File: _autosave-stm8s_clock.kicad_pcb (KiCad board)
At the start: 2 copper layers, 157 parts, among them J1 Conn_01x04, J2 PS, Q1 BC847, Q10 BC847, Q11 BC847, Q12 BC847, Q13 BC847, Q14 BC847, Q15 BC847, Q16 BC847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

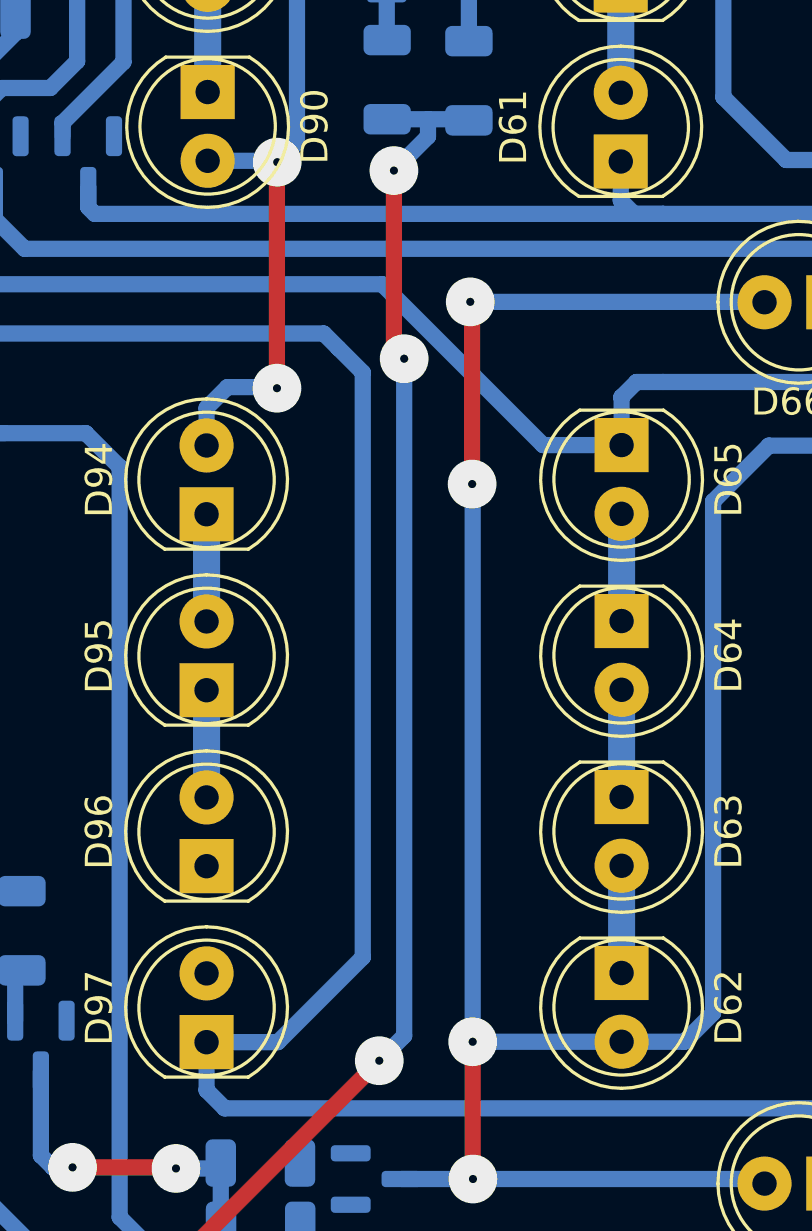
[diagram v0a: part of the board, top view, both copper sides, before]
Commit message: connect to all segment and each digit or shift register to connect each other
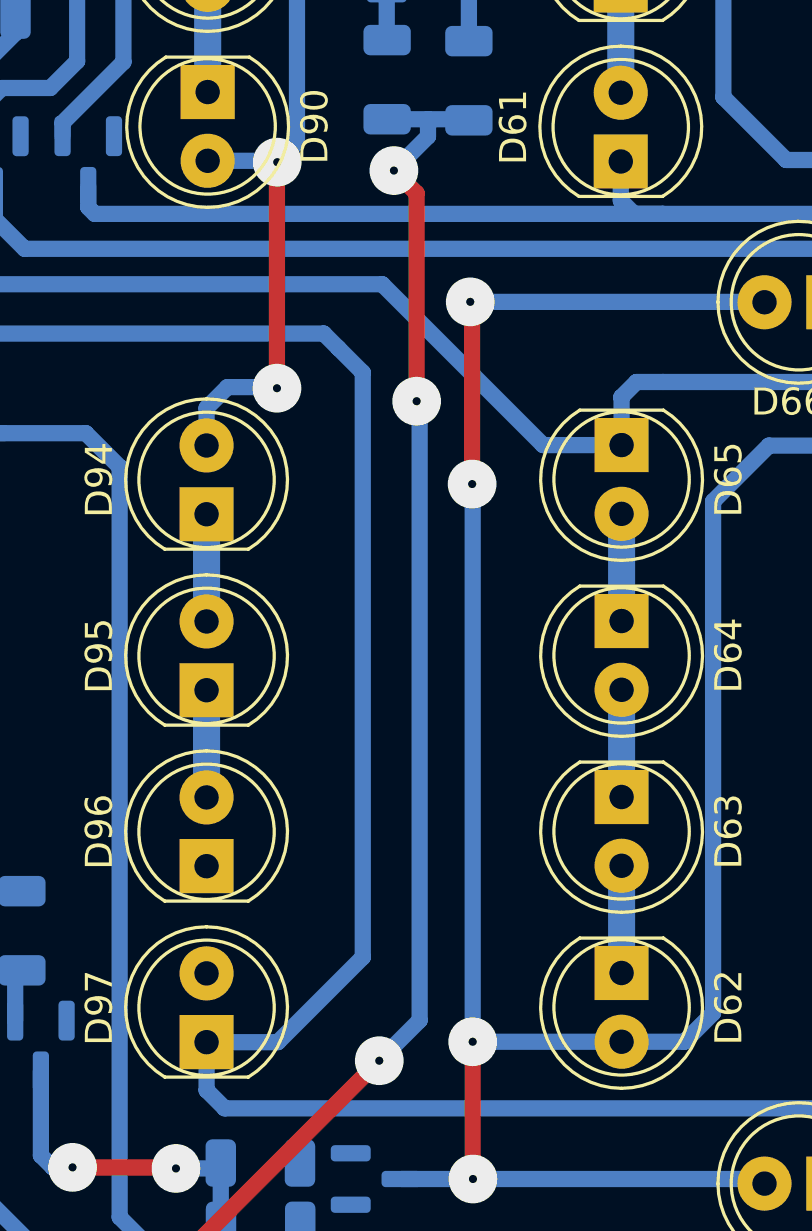
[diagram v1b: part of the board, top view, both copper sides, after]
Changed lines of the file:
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@@
 		(tags "TSSOP SO")
 		(property "Reference" "U1"
-			(at 0 4.2 360)
+			(at 0 4.2 0)
 			(layer "B.SilkS")
 			(effects
@@
 		)
 		(property "Value" "STM8S003F3P"
-			(at 0 -4.2 360)
+			(at 0 -4.2 0)
 			(layer "B.Fab")
 			(effects
@@
 		)
 		(property "Footprint" "Package_SO:TSSOP-20_4.4x6.5mm_P0.65mm"
-			(at 0 0 360)
+			(at 0 0 0)
 			(layer "B.Fab")
 			(hide yes)
@@
 		)
 		(property "Datasheet" "http://www.st.com/st-web-ui/static/active/en/resource/technical/document/datasheet/DM00024550.pdf"
-			(at 0 0 360)
+			(at 0 0 0)
 			(layer "B.Fab")
 			(hide yes)
@@
 		)
 		(property "Description" ""
-			(at 0 0 360)
+			(at 0 0 0)
 			(layer "B.Fab")
 			(hide yes)
@@
 		)
 		(fp_text user "${REFERENCE}"
-			(at 0.2375 1.025 360)
+			(at 0.2375 1.025 0)
 			(layer "B.Fab")
 			(effects
@@
 	)
 	(segment
-		(start 103.02 91.1)
-		(end 103.4 91.48)
+		(start 95 124.89)
+		(end 85.42 124.89)
 		(width 0.6)
 		(layer "F.Cu")
@@
 	)
 	(segment
-		(start 103.02 84.53)
-		(end 103.02 91.1)
+		(start 103.86 85.37)
+		(end 103.02 84.53)
 		(width 0.6)
 		(layer "F.Cu")
@@
 	)
 	(segment
-		(start 95 124.89)
-		(end 85.42 124.89)
+		(start 103.86 93.05)
+		(end 103.86 85.37)
 		(width 0.6)
 		(layer "F.Cu")
@@
 	)
 	(via
-		(at 103.4 91.48)
+		(at 103.86 93.05)
 		(size 1.8)
 		(drill 0.3)
@@
 	)
 	(segment
-		(start 103.4 116.49)
-		(end 102.48 117.41)
-		(width 0.6)
-		(layer "B.Cu")
-		(net 104)
-	)
-	(segment
 		(start 79.48 120.6)
 		(end 79.48 117.815)
@@
 	)
 	(segment
-		(start 103.4 91.48)
-		(end 103.4 116.49)
-		(width 0.6)
-		(layer "B.Cu")
-		(net 104)
-	)
-	(segment
 		(start 102.77 82.635)
 		(end 104.28 82.635)
@@
 		(width 0.6)
 		(layer "B.Cu")
+		(net 104)
+	)
+	(segment
+		(start 103.97 115.92)
+		(end 102.48 117.41)
+		(width 0.6)
+		(layer "B.Cu")
+		(net 104)
+	)
+	(segment
+		(start 103.86 93.05)
+		(end 103.97 93.16)
+		(width 0.6)
+		(layer "B.Cu")
+		(net 104)
+	)
+	(segment
+		(start 103.97 93.16)
+		(end 103.97 115.92)
+		(width 0.6)
+		(layer "B.Cu")
